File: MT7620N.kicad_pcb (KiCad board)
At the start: 2 copper layers, 48 x 45.8 mm, 114 parts, among them IC1 IC_ATMEGA32U4_TQFP44, J1 IO_USB-MICRO-B-MK5P, P2 IO_HOLE-3.2, P3 IO_HOLE-3.2, Q1 AO3416, Q2 AO3416, T1 AO3415, U1 IC_MP1484EN_SOIC08, U10 DLW21SN900SQ2, U13 IP4220CZ6, U14 IP4220CZ6, U15 AP2146, U16 AP2146, U2 DLW21SN900SQ2, U3 IP4220CZ6, U4 UPD720114-QFP48, U5 USB-AF-90, U9 DLW21SN900SQ2, X1 30MHz, X2 16m

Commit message: 整理到根目录
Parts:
- removed the G*** at (130.0, 55.0)
- removed VAL: WRTNode, WRTNode
- added G***: LOGO, LOGO, B.Cu at (198.2, 63.9)
- added G***: OSHW-logo_silkscreen-back_7mm, OSHW-logo_silkscreen-back_7mm, F.Cu at (168.1, 54.5)
- added G***: LOGO, LOGO, F.Cu at (166.1, 67.0)
- added G***: LOGO, LOGO, F.Cu at (168.5, 63.4)
- added JP10: IO_M02X1, IO_M02X1, F.Cu at (162.8, 94.1)
- added JP11: IO_M02X1, IO_M02X1, F.Cu at (162.8, 50.9)
- added JP8: IO_M02X1, IO_M02X1, F.Cu at (160.3, 91.6)
- added JP9: IO_M02X1, IO_M02X1, F.Cu at (162.8, 53.5)
- JP3: value IO_M05X2 -> IO_M02X1; footprint IO_M05X2 -> IO_M02X1
- moved JP3 5.68 mm to (162.8, 89.0), turned to 0 degrees
- moved JP4 5.08 mm to (160.3, 56.0)
- moved C36 0.27 mm to (175.5, 57.8)
- moved R27 0.25 mm to (170.3, 70.2)
- moved R2 0.23 mm to (173.6, 66.7)
- moved R22 0.23 mm to (168.8, 78.8)
- moved C27 0.20 mm to (168.8, 80.7)
- moved C14 0.15 mm to (172.2, 66.0)
- moved C7 0.08 mm to (173.4, 64.8)
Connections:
- JP1 pad 10: /SPI_MOSI -> (no net)
- JP1 pad 11: /SPI_WP -> (no net)
- JP1 pad 12: /SPI_HOLD -> (no net)
- JP1 pad 13: /SPI_CLK -> (no net)
- JP1 pad 14: /SPI_CS1 -> (no net)
- JP1 pad 25: (no net) -> /LINK3
- JP1 pad 26: (no net) -> /LINK4
- JP1 pad 9: /SPI_MISO -> (no net)
- JP3 pad 1: /WRT33V -> GND
- JP3 pad 2: GND -> /WRT33V
- JP4 pad 10: /ATMEGA32U4/IO10* -> /ATMEGA32U4/D5*
- JP4 pad 11: /ATMEGA32U4/IO11* -> /ATMEGA32U4/IO13*
- JP4 pad 12: /ATMEGA32U4/IO12 -> /ATMEGA32U4/D7
- JP4 pad 13: /ATMEGA32U4/IO13* -> /ATMEGA32U4/IO11*
- JP4 pad 5: /ATMEGA32U4/D5* -> /ATMEGA32U4/IO12
- JP4 pad 7: /ATMEGA32U4/D7 -> /ATMEGA32U4/IO8
- JP4 pad 8: /ATMEGA32U4/IO8 -> /ATMEGA32U4/IO9*
- JP4 pad 9: /ATMEGA32U4/IO9* -> /ATMEGA32U4/IO10*
- R26 pad 2: /MCU5V -> +5V
- U4 pad 28: (no net) -> N-0000090
- U4 pad 29: (no net) -> N-0000089
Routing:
- net GND: track 58.5 -> 343.9 mm, vias 0 -> 40
- net +5V: track 46.7 -> 194.5 mm, vias 0 -> 12
- net /WRT33V: track 4.24 -> 84.4 mm, vias 0 -> 6
- net /uPD720114/DP-: track 0.00 -> 59.5 mm, vias 0 -> 1
- net /uPD720114/DP+: track 0.00 -> 57.8 mm, vias 0 -> 1
- net /uPD720114/HUB33V: track 55.7 -> 100.2 mm, vias 0 -> 8
- net /ATMEGA32U4/MCU5V: track 19.6 -> 64.0 mm, vias 0 -> 3
- net /I2C_SCLK: track 0.00 -> 44.2 mm, vias 0 -> 2
- net /ATMEGA32U4/D2/SDA: track 0.00 -> 42.9 mm, vias 0 -> 1
- net +3.3V: track 34.3 -> 77.0 mm, vias 0 -> 2
- net /ATMEGA32U4/D7: track 0.00 -> 40.7 mm, vias 0 -> 3
- net N-0000090: track 0.00 -> 39.9 mm, vias 0 -> 3
- net /uPD720114/VBUS1: track 31.4 -> 69.9 mm
- net /ATMEGA32U4/D3/SCL: track 0.00 -> 37.9 mm, vias 0 -> 3
- net /ATMEGA32U4/D0/RX: track 0.00 -> 37.7 mm
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- added copper zone on B.Cu, net GND
- added copper zone on F.Cu, net N-0000022
- removed copper zone on F.Cu, net N-0000019
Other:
- board size 48 x 45.8 mm -> 48.2 x 45.8 mm
- board text added: "HUB3V3"
- board text added: "WRT3V3"
- board text removed: "-"
- board text removed: "3.3V"
- board text removed: "5V/2A"
- board text removed: "CLK"
- board text removed: "CS1"
- board text removed: "D+"
- board text removed: "D-"
- board text removed: "GPIO0"
- board text removed: "HOLD"
- board text removed: "HUB33V"
- board text removed: "L4"
- board text removed: "L5"
- board text removed: "LK0"
- board text removed: "LK1"
- board text removed: "LK2"
- board text removed: "LK3"
- board text removed: "LK4"
- board text removed: "MISO"
- board text removed: "MOSI"
- board text removed: "PG0"
- board text removed: "PG1"
- board text removed: "RN0"
- board text removed: "RN1"
- board text removed: "RN2"
- board text removed: "RN3"
- board text removed: "RN4"
- board text removed: "RP0"
- board text removed: "RP1"
- board text removed: "RP2"
- board text removed: "RP3"
- board text removed: "RP4"
- board text removed: "RST"
- board text removed: "RXD2"
- board text removed: "SCLK"
- board text removed: "SD"
- board text removed: "TN0"
- board text removed: "TN1"
- board text removed: "TN2"
- board text removed: "TN3"
- board text removed: "TN4"
- board text removed: "TP0"
- board text removed: "TP1"
- board text removed: "TP2"
- board text removed: "TP3"
- board text removed: "TP4"
- board text removed: "TRN"
- board text removed: "TRNB"
- board text removed: "TXD2"
- board text removed: "WAN/LAN"
- board text removed: "WLED"
- board text removed: "WP"
- board text removed: "WRT33V"

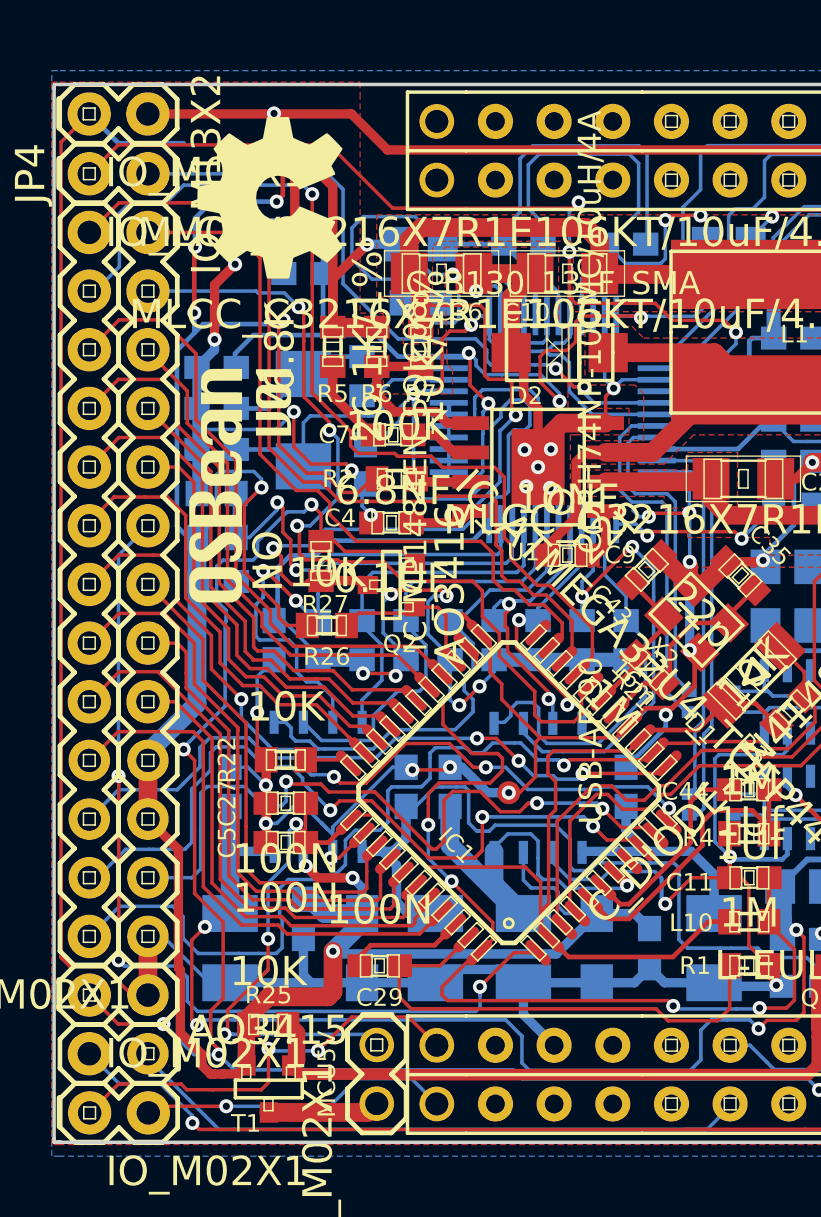
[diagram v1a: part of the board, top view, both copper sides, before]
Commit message: 保存AREF引脚没外引版本
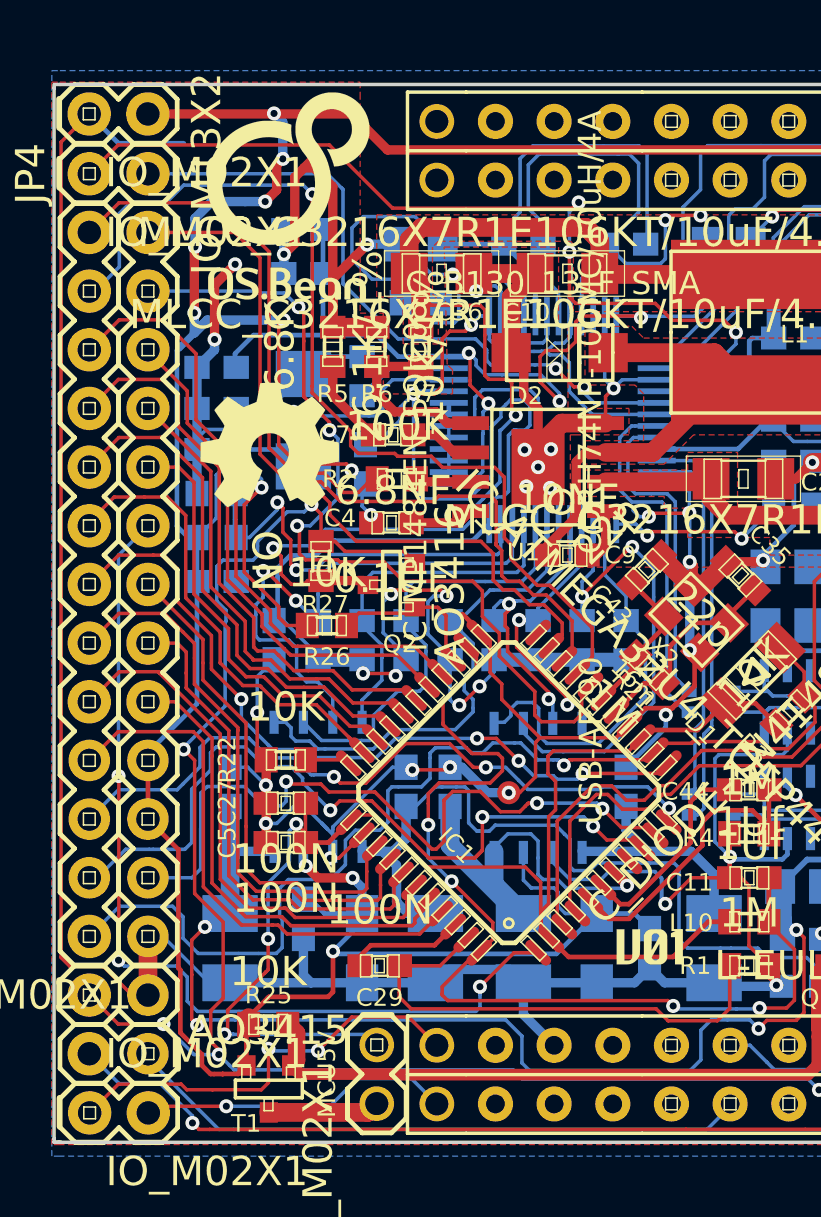
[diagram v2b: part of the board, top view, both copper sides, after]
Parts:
- removed the G*** at (168.1, 54.5)
- removed the G*** at (166.1, 67.0)
- removed the G*** at (168.5, 63.4)
- added G***: OSHW-logo_silkscreen-front_6mm, OSHW-logo_silkscreen-front_6mm, F.Cu at (168.1, 65.2)
- added G***: LOGO, LOGO, F.Cu at (184.5, 87.2)
- added VAL: REF, OSB2, F.Cu at (168.9, 54.5)

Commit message: 生成gerber文件并整理目录
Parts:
- removed the G*** at (168.1, 65.2)
- added G***: OSHW-logo_silkscreen-back_5mm, OSHW-logo_silkscreen-back_5mm, F.Cu at (167.0, 62.1)
- added R28: NO, C_R_0603, B.Cu at (168.0, 93.2)
- moved VAL 1.45 mm to (167.5, 55.0)
- moved P2 0.64 mm to (205.0, 87.0)
- moved G*** 0.58 mm to (184.4, 86.6)
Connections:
- JP4 pad 20: +5V -> /ATMEGA32U4/AREF
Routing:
- net /ATMEGA32U4/AREF: track 4.98 -> 22.0 mm
- net +5V: track 194.3 -> 198.0 mm, vias 12 -> 14
- net /MCU5V: track 4.83 -> 6.51 mm, vias 0 -> 1
- net /ATMEGA32U4/RESET: track 46.3 -> 48.0 mm
- net /ATMEGA32U4/A5: track 23.4 -> 25.0 mm
- net /ATMEGA32U4/MISO: track 30.4 -> 31.6 mm
- net /ATMEGA32U4/D7: track 40.7 -> 41.6 mm
- net /LINK4: track 13.6 -> 14.1 mm
- added copper zone on F.Cu, net N-0000018
- removed copper zone on F.Cu, net N-0000021
